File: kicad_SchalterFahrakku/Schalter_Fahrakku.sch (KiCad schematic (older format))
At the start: 15 parts, among them P1 V_IN+, P2 V_IN-, P3 uC_IN, P4 V_OUT+, P5 V_OUT+, Q1 IRLML6344, Q2 IPD90P03

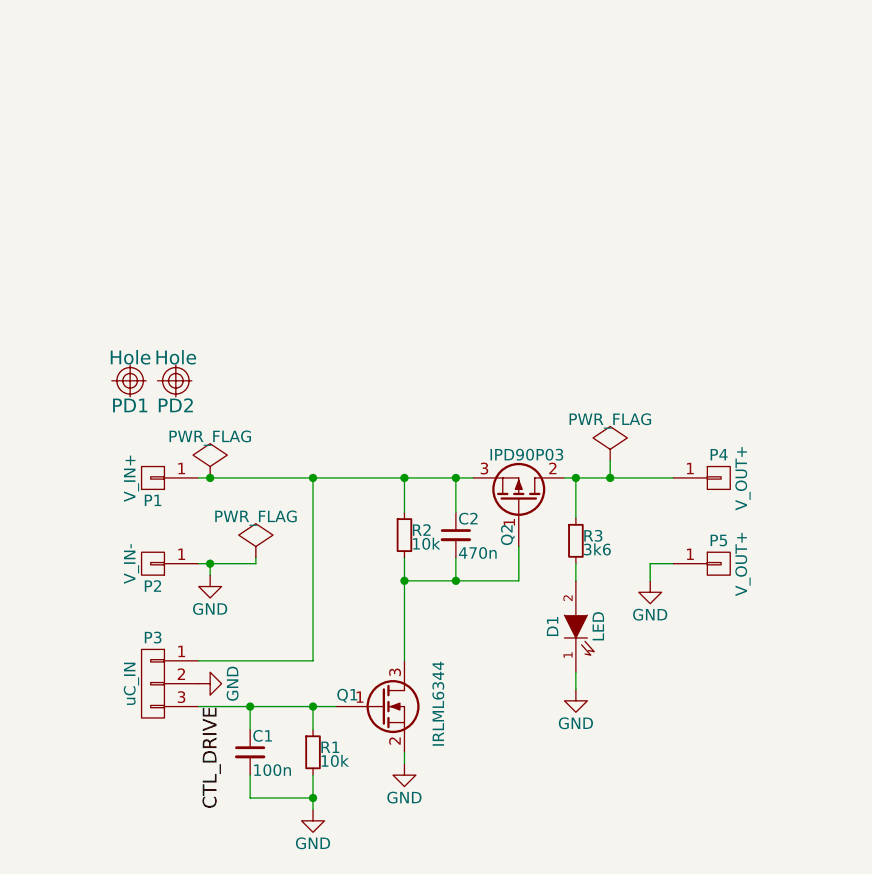
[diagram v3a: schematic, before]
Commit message: - Layout Schalterplatine ohne Routing
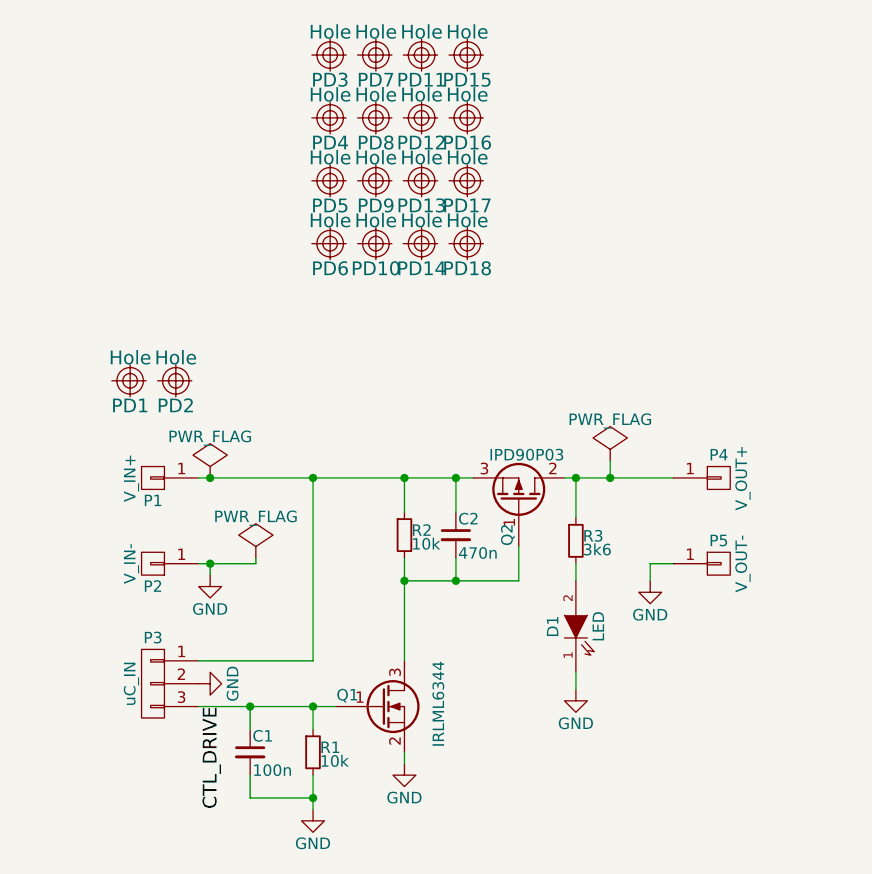
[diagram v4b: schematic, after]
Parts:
- added PD10, PD11, PD12, PD13, PD14, PD15, PD16, PD17, PD18, PD3, PD4, PD5, PD6, PD7, PD8, PD9: Hole, Custom:Hole_3mm, symbol Hole
- P3: footprint Custom:PS25_3W_BR -> Custom:PS25_3W
- P5: value V_OUT+ -> V_OUT-
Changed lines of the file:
@@
 F 0 "P3" H 3750 4000 50  0000 C CNN
 F 1 "uC_IN" V 3850 3800 50  0000 C CNN
-F 2 "Custom:PS25_3W_BR" H 3750 3800 50  0001 C CNN
+F 2 "Custom:PS25_3W" H 3750 3800 50  0001 C CNN
 F 3 "http://cdn-reichelt.de/documents/datenblatt/C151/PS25_xxWBR.pdf" H 3750 3800 50  0001 C CNN
 F 4 "Reichelt" H 3750 3800 60  0001 C CNN "Supply"
@@
 P 6225 3275
 F 0 "P5" H 6225 3375 50  0000 C CNN
-F 1 "V_OUT+" V 6325 3275 50  0000 C CNN
+F 1 "V_OUT-" V 6325 3275 50  0000 C CNN
 F 2 "Custom:Pad_SMD_3.5x10" H 6225 3275 50  0001 C CNN
 F 3 "" H 6225 3275 50  0000 C CNN
@@
 	5600 3075 5600 2900
 Connection ~ 5600 2900
+$Comp
+L Hole PD6
+U 1 1 57C82B56
+P 4525 1875
+F 0 "PD6" H 4525 1765 60  0000 C CNN
+F 1 "Hole" H 4525 1975 60  0000 C CNN
+F 2 "Custom:Hole_3mm" H 4525 1875 60  0001 C CNN
+F 3 "" H 4525 1875 60  0000 C CNN
+	1    4525 1875
+	1    0    0    -1
+$EndComp
+$Comp
+L Hole PD10
+U 1 1 57C82C3B
+P 4725 1875
+F 0 "PD10" H 4725 1765 60  0000 C CNN
+F 1 "Hole" H 4725 1975 60  0000 C CNN
+F 2 "Custom:Hole_3mm" H 4725 1875 60  0001 C CNN
+F 3 "" H 4725 1875 60  0000 C CNN
+	1    4725 1875
+	1    0    0    -1
+$EndComp
+$Comp
+L Hole PD14
+U 1 1 57C82C86
+P 4925 1875
+F 0 "PD14" H 4925 1765 60  0000 C CNN
+F 1 "Hole" H 4925 1975 60  0000 C CNN
+F 2 "Custom:Hole_3mm" H 4925 1875 60  0001 C CNN
+F 3 "" H 4925 1875 60  0000 C CNN
+	1    4925 1875
+	1    0    0    -1
+$EndComp
+$Comp
+L Hole PD18
+U 1 1 57C82CD8
+P 5125 1875
+F 0 "PD18" H 5125 1765 60  0000 C CNN
+F 1 "Hole" H 5125 1975 60  0000 C CNN
+F 2 "Custom:Hole_3mm" H 5125 1875 60  0001 C CNN
+F 3 "" H 5125 1875 60  0000 C CNN
+	1    5125 1875
+	1    0    0    -1
+$EndComp
+$Comp
+L Hole PD5
+U 1 1 57C82E3F
+P 4525 1600
+F 0 "PD5" H 4525 1490 60  0000 C CNN
+F 1 "Hole" H 4525 1700 60  0000 C CNN
+F 2 "Custom:Hole_3mm" H 4525 1600 60  0001 C CNN
+F 3 "" H 4525 1600 60  0000 C CNN
+	1    4525 1600
+	1    0    0    -1
+$EndComp
+$Comp
+L Hole PD9
+U 1 1 57C82F3D
+P 4725 1600
+F 0 "PD9" H 4725 1490 60  0000 C CNN
+F 1 "Hole" H 4725 1700 60  0000 C CNN
+F 2 "Custom:Hole_3mm" H 4725 1600 60  0001 C CNN
+F 3 "" H 4725 1600 60  0000 C CNN
+	1    4725 1600
+	1    0    0    -1
+$EndComp
+$Comp
+L Hole PD13
+U 1 1 57C82F98
+P 4925 1600
+F 0 "PD13" H 4925 1490 60  0000 C CNN
+F 1 "Hole" H 4925 1700 60  0000 C CNN
+F 2 "Custom:Hole_3mm" H 4925 1600 60  0001 C CNN
+F 3 "" H 4925 1600 60  0000 C CNN
+	1    4925 1600
+	1    0    0    -1
+$EndComp
+$Comp
+L Hole PD17
+U 1 1 57C82FFA
+P 5125 1600
+F 0 "PD17" H 5125 1490 60  0000 C CNN
+F 1 "Hole" H 5125 1700 60  0000 C CNN
+F 2 "Custom:Hole_3mm" H 5125 1600 60  0001 C CNN
+F 3 "" H 5125 1600 60  0000 C CNN
+	1    5125 1600
+	1    0    0    -1
+$EndComp
+$Comp
+L Hole PD4
+U 1 1 57C83063
+P 4525 1325
+F 0 "PD4" H 4525 1215 60  0000 C CNN
+F 1 "Hole" H 4525 1425 60  0000 C CNN
+F 2 "Custom:Hole_3mm" H 4525 1325 60  0001 C CNN
+F 3 "" H 4525 1325 60  0000 C CNN
+	1    4525 1325
+	1    0    0    -1
+$EndComp
+$Comp
+L Hole PD8
+U 1 1 57C830CB
+P 4725 1325
+F 0 "PD8" H 4725 1215 60  0000 C CNN
+F 1 "Hole" H 4725 1425 60  0000 C CNN
+F 2 "Custom:Hole_3mm" H 4725 1325 60  0001 C CNN
+F 3 "" H 4725 1325 60  0000 C CNN
+	1    4725 1325
+	1    0    0    -1
+$EndComp
+$Comp
+L Hole PD12
+U 1 1 57C83132
+P 4925 1325
+F 0 "PD12" H 4925 1215 60  0000 C CNN
+F 1 "Hole" H 4925 1425 60  0000 C CNN
+F 2 "Custom:Hole_3mm" H 4925 1325 60  0001 C CNN
+F 3 "" H 4925 1325 60  0000 C CNN
+	1    4925 1325
+	1    0    0    -1
+$EndComp
+$Comp
+L Hole PD16
+U 1 1 57C8319C
+P 5125 1325
+F 0 "PD16" H 5125 1215 60  0000 C CNN
+F 1 "Hole" H 5125 1425 60  0000 C CNN
+F 2 "Custom:Hole_3mm" H 5125 1325 60  0001 C CNN
+F 3 "" H 5125 1325 60  0000 C CNN
+	1    5125 1325
+	1    0    0    -1
+$EndComp
+$Comp
+L Hole PD3
+U 1 1 57C83262
+P 4525 1050
+F 0 "PD3" H 4525 940 60  0000 C CNN
+F 1 "Hole" H 4525 1150 60  0000 C CNN
+F 2 "Custom:Hole_3mm" H 4525 1050 60  0001 C CNN
+F 3 "" H 4525 1050 60  0000 C CNN
+	1    4525 1050
+	1    0    0    -1
+$EndComp
+$Comp
+L Hole PD7
+U 1 1 57C832D6
+P 4725 1050
+F 0 "PD7" H 4725 940 60  0000 C CNN
+F 1 "Hole" H 4725 1150 60  0000 C CNN
+F 2 "Custom:Hole_3mm" H 4725 1050 60  0001 C CNN
+F 3 "" H 4725 1050 60  0000 C CNN
+	1    4725 1050
+	1    0    0    -1
+$EndComp
+$Comp
+L Hole PD11
+U 1 1 57C83349
+P 4925 1050
+F 0 "PD11" H 4925 940 60  0000 C CNN
+F 1 "Hole" H 4925 1150 60  0000 C CNN
+F 2 "Custom:Hole_3mm" H 4925 1050 60  0001 C CNN
+F 3 "" H 4925 1050 60  0000 C CNN
+	1    4925 1050
+	1    0    0    -1
+$EndComp
+$Comp
+L Hole PD15
+U 1 1 57C833BD
+P 5125 1050
+F 0 "PD15" H 5125 940 60  0000 C CNN
+F 1 "Hole" H 5125 1150 60  0000 C CNN
+F 2 "Custom:Hole_3mm" H 5125 1050 60  0001 C CNN
+F 3 "" H 5125 1050 60  0000 C CNN
+	1    5125 1050
+	1    0    0    -1
+$EndComp
 $EndSCHEMATC
